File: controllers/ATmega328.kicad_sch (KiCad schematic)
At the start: 10 parts, among them U401 ATMEGA328P-AU, Y407 16MHz

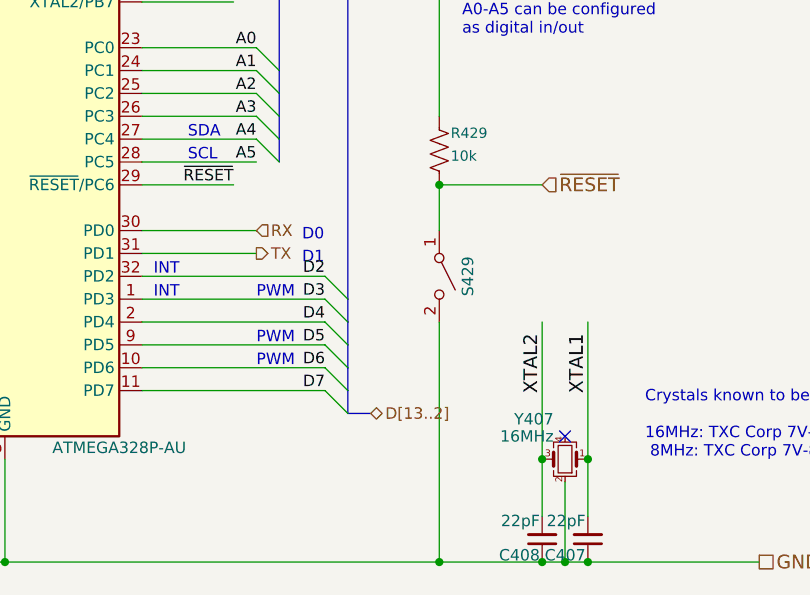
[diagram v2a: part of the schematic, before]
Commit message: Change to 8MHz crystal
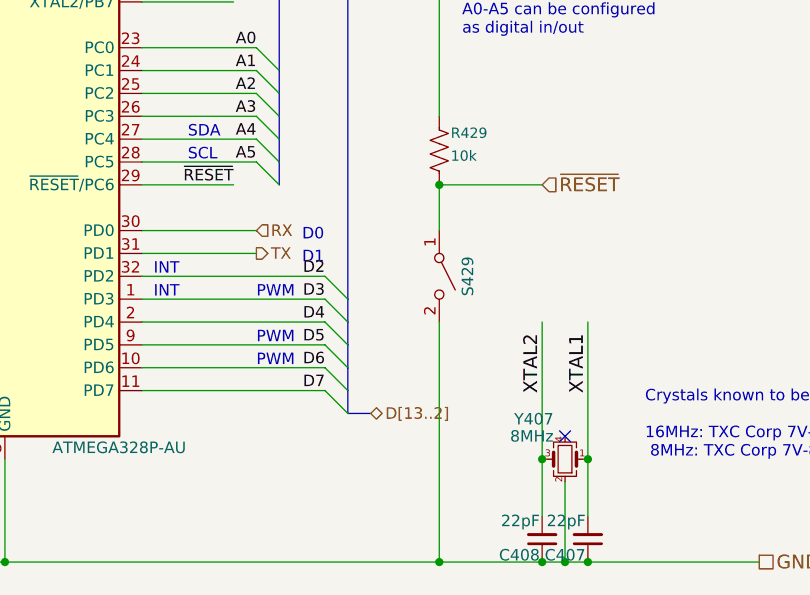
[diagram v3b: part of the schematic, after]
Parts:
- C404, C406: Part Number (none) -> CGA2B1X7R1C104K050BC; Purpose (none) -> Microcontroller VCC bypass
- C407, C408: Part Number (none) -> CGA2B2C0G1H220J050BA; Purpose (none) -> Crystal load capacitor
- C418: Part Number (none) -> CGA2B1X7R1C104K050BC; Purpose (none) -> Microcontroller analog bypass
- C420: Part Number (none) -> CGA2B1X7R1C104K050BC; Purpose (none) -> Microcontroller aref bypass
- R429: Part Number (none) -> ERJ-PA2J103X; Purpose (none) -> Pullup resistor
- S429: Part Number (none) -> B3U-1000P; Purpose (none) -> Reset button
- U401: Digikey ATMEGA328P-15AZCT-ND -> ATMEGA328P-AURCT-ND; Part Number (none) -> ATMEGA328P-AUR; Purpose (none) -> Microcontroller
- Y407: value 16MHz -> 8MHz; Digikey 887-1800-1-ND -> 887-7V-8.000MDDQ-TCT-ND; Part Number (none) -> 7V-8.000MDDQ-T; Purpose (none) -> Microcontroller crystal
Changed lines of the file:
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@@
+    (stroke (width 0) (type default))
+  )
+  (bus_entry (at 104.14 68.58) (size 2.54 2.54)
     (stroke (width 0) (type default))
   )
@@
   )
   (bus (pts (xy 106.68 22.86) (xy 54.61 22.86))
+    (stroke (width 0) (type default))
+  )
+  (bus (pts (xy 106.68 68.58) (xy 106.68 71.12))
     (stroke (width 0) (type default))
   )
@@
       (effects (font (size 1.27 1.27)) hide)
     )
-    (property "Datasheet" "" (at 38.1 52.07 0)
+    (property "Datasheet" "https://product.tdk.com/system/files/dam/doc/product/capacitor/ceramic/mlcc/catalog/mlcc_automotive_general_en.pdf" (at 38.1 52.07 0)
       (effects (font (size 1.27 1.27)) hide)
     )
@@
       (effects (font (size 1.524 1.524)) hide)
     )
+    (property "Part Number" "CGA2B1X7R1C104K050BC" (at 38.1 52.07 0)
+      (effects (font (size 1.27 1.27)) hide)
+    )
+    (property "Purpose" "Microcontroller aref bypass" (at 38.1 52.07 0)
+      (effects (font (size 1.27 1.27)) hide)
+    )
     (pin "1")
     (pin "2")
@@
       )
       (project "Precision23"
-        (path "/9151f981-b383-4946-8df4-92ef46ef2206/84662bc9-aa4f-4f0d-8756-174283206cf9"
+        (path "/9151f981-b383-4946-8df4-92ef46ef2206/9f66be35-2744-413f-8b31-a996047a434b/84662bc9-aa4f-4f0d-8756-174283206cf9"
           (reference "C420") (unit 1)
         )
@@
       (effects (font (size 1.27 1.27)) hide)
     )
-    (property "Datasheet" "" (at 27.94 45.72 0)
+    (property "Datasheet" "https://product.tdk.com/system/files/dam/doc/product/capacitor/ceramic/mlcc/catalog/mlcc_automotive_general_en.pdf" (at 27.94 45.72 0)
       (effects (font (size 1.27 1.27)) hide)
     )
@@
       (effects (font (size 1.524 1.524)) hide)
     )
+    (property "Part Number" "CGA2B1X7R1C104K050BC" (at 27.94 45.72 0)
+      (effects (font (size 1.27 1.27)) hide)
+    )
+    (property "Purpose" "Microcontroller analog bypass" (at 27.94 45.72 0)
+      (effects (font (size 1.27 1.27)) hide)
+    )
     (pin "1")
     (pin "2")
@@
       )
       (project "Precision23"
-        (path "/9151f981-b383-4946-8df4-92ef46ef2206/84662bc9-aa4f-4f0d-8756-174283206cf9"
+        (path "/9151f981-b383-4946-8df4-92ef46ef2206/9f66be35-2744-413f-8b31-a996047a434b/84662bc9-aa4f-4f0d-8756-174283206cf9"
           (reference "C418") (unit 1)
         )
@@
       (effects (font (size 1.27 1.27)) hide)
     )
-    (property "Datasheet" "" (at 25.4 52.07 0)
+    (property "Datasheet" "https://product.tdk.com/system/files/dam/doc/product/capacitor/ceramic/mlcc/catalog/mlcc_automotive_general_en.pdf" (at 25.4 52.07 0)
       (effects (font (size 1.27 1.27)) hide)
     )
@@
       (effects (font (size 1.524 1.524)) hide)
     )
+    (property "Part Number" "CGA2B1X7R1C104K050BC" (at 25.4 52.07 0)
+      (effects (font (size 1.27 1.27)) hide)
+    )
+    (property "Purpose" "Microcontroller VCC bypass" (at 25.4 52.07 0)
+      (effects (font (size 1.27 1.27)) hide)
+    )
     (pin "1")
     (pin "2")
@@
       )
       (project "Precision23"
-        (path "/9151f981-b383-4946-8df4-92ef46ef2206/84662bc9-aa4f-4f0d-8756-174283206cf9"
+        (path "/9151f981-b383-4946-8df4-92ef46ef2206/9f66be35-2744-413f-8b31-a996047a434b/84662bc9-aa4f-4f0d-8756-174283206cf9"
           (reference "C406") (unit 1)
         )
@@
       (effects (font (size 1.27 1.27)) hide)
     )
-    (property "Datasheet" "" (at 22.86 58.42 0)
+    (property "Datasheet" "https://product.tdk.com/system/files/dam/doc/product/capacitor/ceramic/mlcc/catalog/mlcc_automotive_general_en.pdf" (at 22.86 58.42 0)
       (effects (font (size 1.27 1.27)) hide)
     )
@@
       (effects (font (size 1.524 1.524)) hide)
     )
+    (property "Part Number" "CGA2B1X7R1C104K050BC" (at 22.86 58.42 0)
+      (effects (font (size 1.27 1.27)) hide)
+    )
+    (property "Purpose" "Microcontroller VCC bypass" (at 22.86 58.42 0)
+      (effects (font (size 1.27 1.27)) hide)
+    )
     (pin "1")
     (pin "2")
@@
       )
       (project "Precision23"
-        (path "/9151f981-b383-4946-8df4-92ef46ef2206/84662bc9-aa4f-4f0d-8756-174283206cf9"
+        (path "/9151f981-b383-4946-8df4-92ef46ef2206/9f66be35-2744-413f-8b31-a996047a434b/84662bc9-aa4f-4f0d-8756-174283206cf9"
           (reference "C404") (unit 1)
         )
@@
       (effects (font (size 1.27 1.27)) (justify left))
     )
-    (property "Value" "16MHz" (at 137.16 99.06 0)
+    (property "Value" "8MHz" (at 137.16 99.06 0)
       (effects (font (size 1.27 1.27)) (justify left))
     )
@@
       (effects (font (size 1.27 1.27)) hide)
     )
-    (property "Digikey" "887-1800-1-ND" (at 138.43 101.6 0)
-      (effects (font (size 1.524 1.524)) hide)
+    (property "Digikey" "887-7V-8.000MDDQ-TCT-ND" (at 138.43 101.6 0)
+      (effects (font (size 1.524 1.524)) hide)
+    )
+    (property "Part Number" "7V-8.000MDDQ-T" (at 138.43 101.6 0)
+      (effects (font (size 1.27 1.27)) hide)
+    )
+    (property "Purpose" "Microcontroller crystal" (at 138.43 101.6 0)
+      (effects (font (size 1.27 1.27)) hide)
     )
     (pin "1")
@@
       )
       (project "Precision23"
-        (path "/9151f981-b383-4946-8df4-92ef46ef2206/84662bc9-aa4f-4f0d-8756-174283206cf9"
+        (path "/9151f981-b383-4946-8df4-92ef46ef2206/9f66be35-2744-413f-8b31-a996047a434b/84662bc9-aa4f-4f0d-8756-174283206cf9"
           (reference "Y407") (unit 1)
         )
@@
       (effects (font (size 1.27 1.27)) hide)
     )
-    (property "Datasheet" "" (at 140.97 110.49 0)
+    (property "Datasheet" "https://product.tdk.com/system/files/dam/doc/product/capacitor/ceramic/mlcc/catalog/mlcc_automotive_general_en.pdf" (at 140.97 110.49 0)
       (effects (font (size 1.27 1.27)) hide)
     )
@@
       (effects (font (size 1.524 1.524)) hide)
     )
+    (property "Part Number" "CGA2B2C0G1H220J050BA" (at 140.97 110.49 0)
+      (effects (font (size 1.27 1.27)) hide)
+    )
+    (property "Purpose" "Crystal load capacitor" (at 140.97 110.49 0)
+      (effects (font (size 1.27 1.27)) hide)
+    )
     (pin "1")
     (pin "2")
@@
       )
       (project "Precision23"
-        (path "/9151f981-b383-4946-8df4-92ef46ef2206/84662bc9-aa4f-4f0d-8756-174283206cf9"
+        (path "/9151f981-b383-4946-8df4-92ef46ef2206/9f66be35-2744-413f-8b31-a996047a434b/84662bc9-aa4f-4f0d-8756-174283206cf9"
           (reference "C407") (unit 1)
         )
@@
       (effects (font (size 1.27 1.27)) hide)
     )
-    (property "Datasheet" "" (at 135.89 110.49 0)
+    (property "Datasheet" "https://product.tdk.com/system/files/dam/doc/product/capacitor/ceramic/mlcc/catalog/mlcc_automotive_general_en.pdf" (at 135.89 110.49 0)
       (effects (font (size 1.27 1.27)) hide)
     )
@@
       (effects (font (size 1.524 1.524)) hide)
     )
+    (property "Part Number" "CGA2B2C0G1H220J050BA" (at 135.89 110.49 0)
+      (effects (font (size 1.27 1.27)) hide)
+    )
+    (property "Purpose" "Crystal load capacitor" (at 135.89 110.49 0)
+      (effects (font (size 1.27 1.27)) hide)
+    )
     (pin "1")
     (pin "2")
@@
       )
       (project "Precision23"
-        (path "/9151f981-b383-4946-8df4-92ef46ef2206/84662bc9-aa4f-4f0d-8756-174283206cf9"
+        (path "/9151f981-b383-4946-8df4-92ef46ef2206/9f66be35-2744-413f-8b31-a996047a434b/84662bc9-aa4f-4f0d-8756-174283206cf9"
           (reference "C408") (unit 1)
         )
@@
       (effects (font (size 1.27 1.27)) hide)
     )
-    (property "Datasheet" "" (at 124.46 81.28 0)
+    (property "Datasheet" "https://omronfs.omron.com/en_US/ecb/products/pdf/en-b3u.pdf" (at 124.46 81.28 0)
       (effects (font (size 1.27 1.27)) hide)
     )
@@
       (effects (font (size 1.524 1.524)) hide)
     )
+    (property "Part Number" "B3U-1000P" (at 124.46 81.28 0)
+      (effects (font (size 1.27 1.27)) hide)
+    )
+    (property "Purpose" "Reset button" (at 124.46 81.28 0)
+      (effects (font (size 1.27 1.27)) hide)
+    )
     (pin "1")
     (pin "2")
@@
       )
       (project "Precision23"
-        (path "/9151f981-b383-4946-8df4-92ef46ef2206/84662bc9-aa4f-4f0d-8756-174283206cf9"
+        (path "/9151f981-b383-4946-8df4-92ef46ef2206/9f66be35-2744-413f-8b31-a996047a434b/84662bc9-aa4f-4f0d-8756-174283206cf9"
           (reference "S429") (unit 1)
         )
@@
       (effects (font (size 0.508 0.508)) hide)
     )
-    (property "Datasheet" "" (at 135.255 74.93 0)
+    (property "Datasheet" "https://industrial.panasonic.com/cdbs/www-data/pdf/RDO0000/AOA0000C331.pdf" (at 135.255 74.93 0)
       (effects (font (size 1.524 1.524)) hide)
     )
@@
       (effects (font (size 1.524 1.524)) hide)
     )
+    (property "Part Number" "ERJ-PA2J103X" (at 124.46 67.31 0)
+      (effects (font (size 1.27 1.27)) hide)
+    )
+    (property "Purpose" "Pullup resistor" (at 124.46 67.31 0)
+      (effects (font (size 1.27 1.27)) hide)
+    )
     (pin "1")
     (pin "2")
@@
       )
       (project "Precision23"
-        (path "/9151f981-b383-4946-8df4-92ef46ef2206/84662bc9-aa4f-4f0d-8756-174283206cf9"
+        (path "/9151f981-b383-4946-8df4-92ef46ef2206/9f66be35-2744-413f-8b31-a996047a434b/84662bc9-aa4f-4f0d-8756-174283206cf9"
           (reference "R429") (unit 1)
         )
@@
       (effects (font (size 1.27 1.27)) hide)
     )
-    (property "Digikey" "ATMEGA328P-15AZCT-ND" (at 76.2 63.5 0)
-      (effects (font (size 1.524 1.524)) hide)
+    (property "Digikey" "ATMEGA328P-AURCT-ND" (at 76.2 63.5 0)
+      (effects (font (size 1.524 1.524)) hide)
+    )
+    (property "Part Number" "ATMEGA328P-AUR" (at 76.2 63.5 0)
+      (effects (font (size 1.27 1.27)) hide)
+    )
+    (property "Purpose" "Microcontroller" (at 76.2 63.5 0)
+      (effects (font (size 1.27 1.27)) hide)
     )
     (pin "1")
@@
       )
       (project "Precision23"
-        (path "/9151f981-b383-4946-8df4-92ef46ef2206/84662bc9-aa4f-4f0d-8756-174283206cf9"
+        (path "/9151f981-b383-4946-8df4-92ef46ef2206/9f66be35-2744-413f-8b31-a996047a434b/84662bc9-aa4f-4f0d-8756-174283206cf9"
           (reference "U401") (unit 1)
         )
